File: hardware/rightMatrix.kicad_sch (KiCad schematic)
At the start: 44 parts, among them J6 MAIN_CONN, J7 CLUSTER_CONN, SW24 MX HotSwap, SW25 MX HotSwap, SW26 MX HotSwap, SW27 MX HotSwap, SW28 MX HotSwap, SW29 MX HotSwap, SW30 MX HotSwap, SW31 MX HotSwap, SW32 MX HotSwap, SW33 MX HotSwap, SW34 MX HotSwap, SW35 MX HotSwap, SW36 MX HotSwap, SW37 MX HotSwap, SW38 MX HotSwap, SW39 MX HotSwap, SW40 MX HotSwap, SW41 MX HotSwap, SW42 MX HotSwap, SW43 MX HotSwap, SW44 MX HotSwap

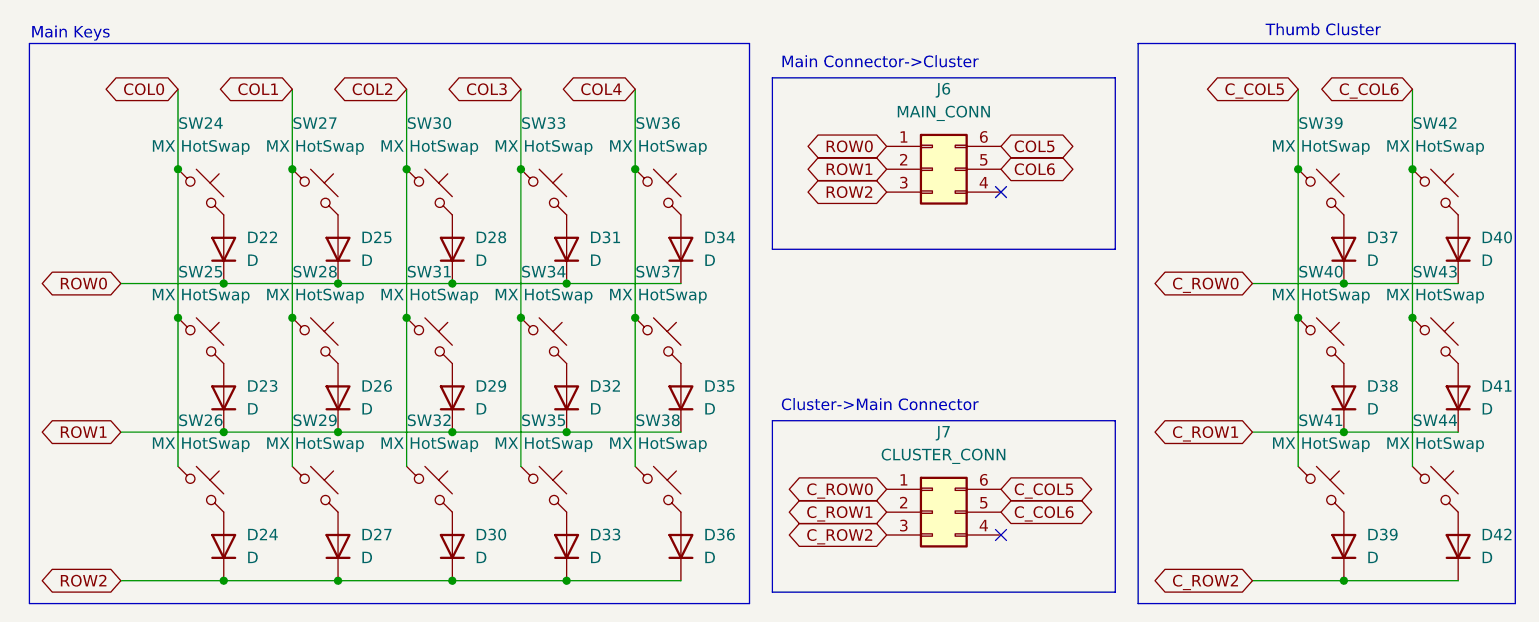
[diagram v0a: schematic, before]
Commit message: started routing left side
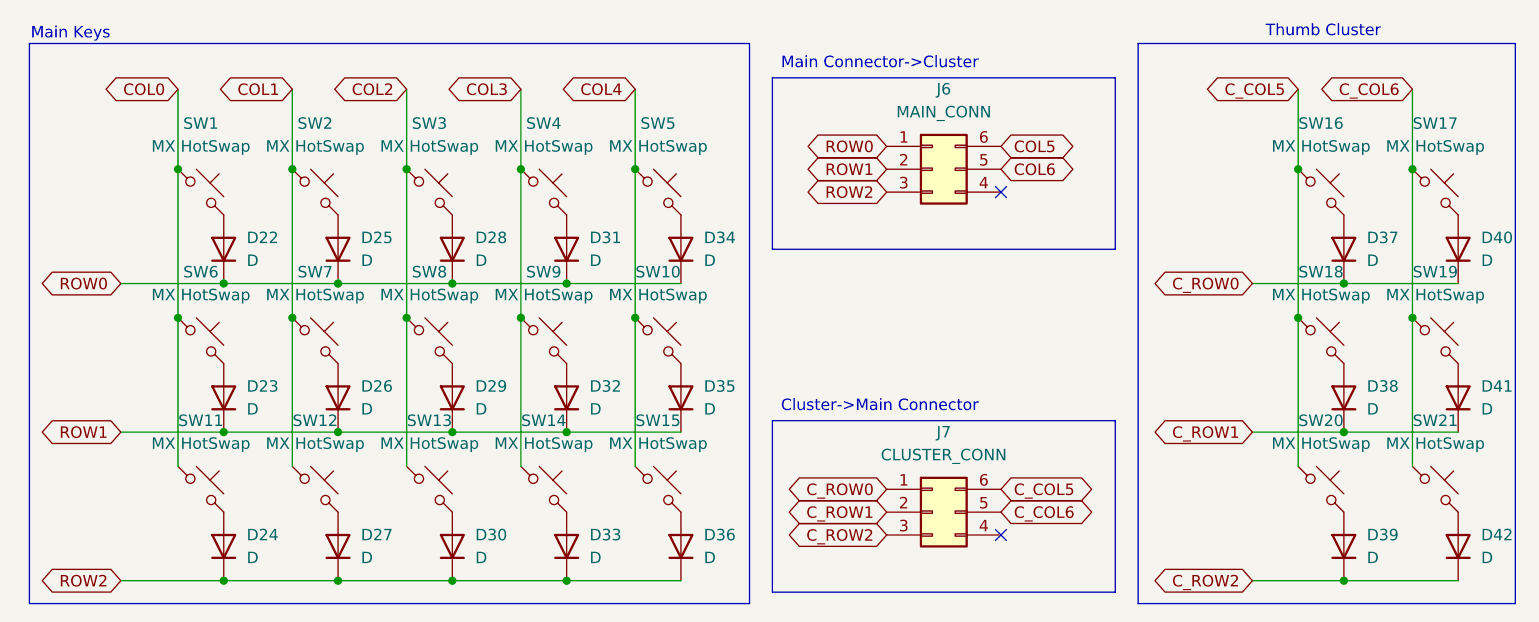
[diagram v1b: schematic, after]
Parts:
- SW1: renamed from SW24; footprint MX_Hotswap:MX-Hotswap-1U -> PCM_marbastlib-mx:SW_MX_HS_CPG151101S11_1u
- SW10: renamed from SW37; footprint MX_Hotswap:MX-Hotswap-1U -> PCM_marbastlib-mx:SW_MX_HS_CPG151101S11_1u
- SW11: renamed from SW26; footprint MX_Hotswap:MX-Hotswap-1U -> PCM_marbastlib-mx:SW_MX_HS_CPG151101S11_1u
- SW12: renamed from SW29; footprint MX_Hotswap:MX-Hotswap-1U -> PCM_marbastlib-mx:SW_MX_HS_CPG151101S11_1u
- SW13: renamed from SW32; footprint MX_Hotswap:MX-Hotswap-1U -> PCM_marbastlib-mx:SW_MX_HS_CPG151101S11_1u
- SW14: renamed from SW35; footprint MX_Hotswap:MX-Hotswap-1U -> PCM_marbastlib-mx:SW_MX_HS_CPG151101S11_1u
- SW15: renamed from SW38; footprint MX_Hotswap:MX-Hotswap-1U -> PCM_marbastlib-mx:SW_MX_HS_CPG151101S11_1u
- SW16: renamed from SW39; footprint MX_Hotswap:MX-Hotswap-1U -> PCM_marbastlib-mx:SW_MX_HS_CPG151101S11_1u
- SW17: renamed from SW42; footprint MX_Hotswap:MX-Hotswap-1U -> PCM_marbastlib-mx:SW_MX_HS_CPG151101S11_1u
- SW18: renamed from SW40; footprint MX_Hotswap:MX-Hotswap-2U -> PCM_marbastlib-mx:SW_MX_HS_CPG151101S11_1u
- SW19: renamed from SW43; footprint MX_Hotswap:MX-Hotswap-1U -> PCM_marbastlib-mx:SW_MX_HS_CPG151101S11_1u
- SW2: renamed from SW27; footprint MX_Hotswap:MX-Hotswap-1U -> PCM_marbastlib-mx:SW_MX_HS_CPG151101S11_1u
- SW20: renamed from SW41; footprint MX_Hotswap:MX-Hotswap-2U -> PCM_marbastlib-mx:SW_MX_HS_CPG151101S11_1u
- SW21: renamed from SW44; footprint MX_Hotswap:MX-Hotswap-1U -> PCM_marbastlib-mx:SW_MX_HS_CPG151101S11_1u
- SW3: renamed from SW30; footprint MX_Hotswap:MX-Hotswap-1U -> PCM_marbastlib-mx:SW_MX_HS_CPG151101S11_1u
- SW4: renamed from SW33; footprint MX_Hotswap:MX-Hotswap-1U -> PCM_marbastlib-mx:SW_MX_HS_CPG151101S11_1u
- SW5: renamed from SW36; footprint MX_Hotswap:MX-Hotswap-1U -> PCM_marbastlib-mx:SW_MX_HS_CPG151101S11_1u
- SW6: renamed from SW25; footprint MX_Hotswap:MX-Hotswap-1U -> PCM_marbastlib-mx:SW_MX_HS_CPG151101S11_1u
- SW7: renamed from SW28; footprint MX_Hotswap:MX-Hotswap-1U -> PCM_marbastlib-mx:SW_MX_HS_CPG151101S11_1u
- SW8: renamed from SW31; footprint MX_Hotswap:MX-Hotswap-1U -> PCM_marbastlib-mx:SW_MX_HS_CPG151101S11_1u
- SW9: renamed from SW34; footprint MX_Hotswap:MX-Hotswap-1U -> PCM_marbastlib-mx:SW_MX_HS_CPG151101S11_1u
